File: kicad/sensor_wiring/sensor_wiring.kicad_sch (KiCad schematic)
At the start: 11 parts

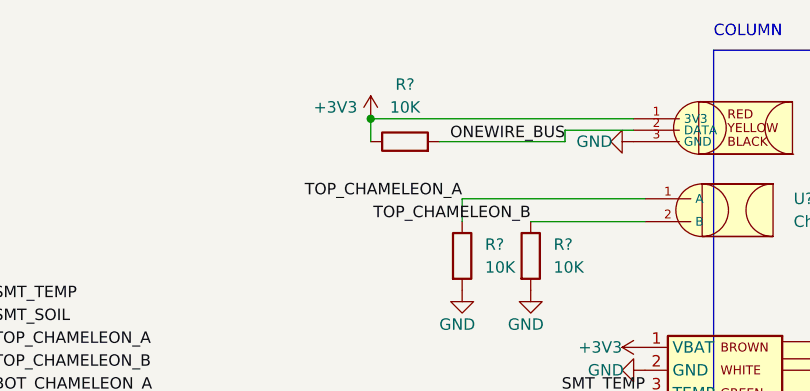
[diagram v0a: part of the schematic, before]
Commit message: Updated wiring and json -> mcap tool
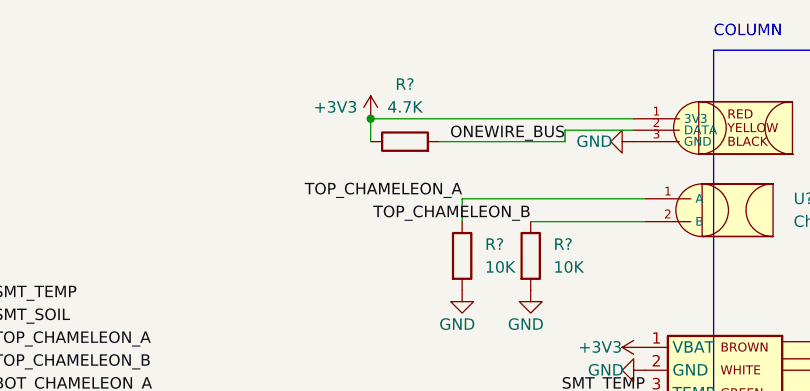
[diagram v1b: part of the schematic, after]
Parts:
- R?: value 10K -> 4.7K
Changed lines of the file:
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@@
     (in_bom yes) (on_board yes) (fields_autoplaced)
     (property "Reference" "R?" (id 0) (at 153.67 44.45 90))
-    (property "Value" "10K" (id 1) (at 153.67 46.99 90))
+    (property "Value" "4.7K" (id 1) (at 153.67 46.99 90))
     (property "Footprint" "" (id 2) (at 153.67 52.578 90)
       (effects (font (size 1.27 1.27)) hide)
@@
     )
     (path "/899fc1a9-69c4-42a8-a9bd-b912cefba171"
-      (reference "R?") (unit 1) (value "10K") (footprint "")
+      (reference "R?") (unit 1) (value "4.7K") (footprint "")
     )
     (path "/972e121d-0436-4bc6-811c-05b349625849"
